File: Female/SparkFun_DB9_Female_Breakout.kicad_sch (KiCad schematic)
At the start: 9 parts, among them J1 DB9-Female, J2 Conn_01x09, J3 Conn_01x01, J4 Conn_01x01

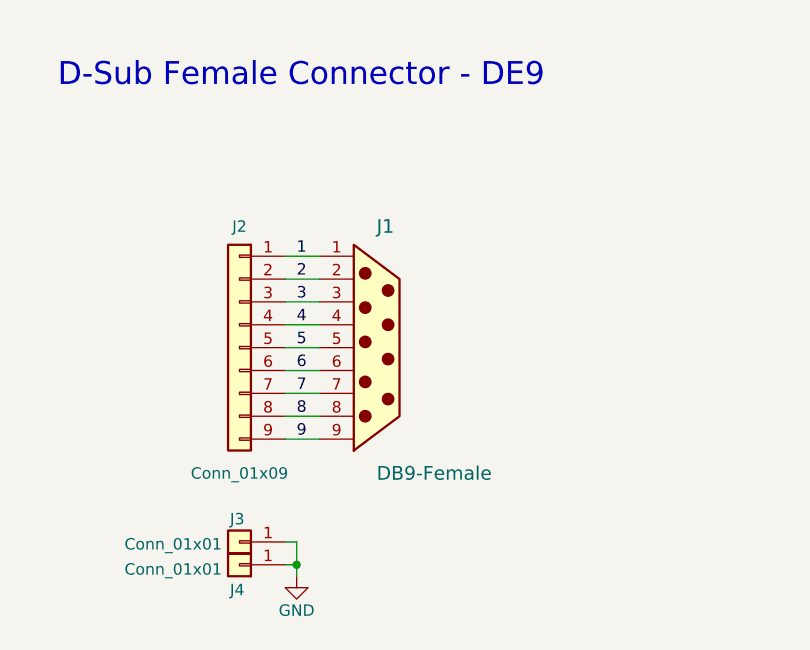
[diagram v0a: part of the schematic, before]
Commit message: Updates DE9 symbol
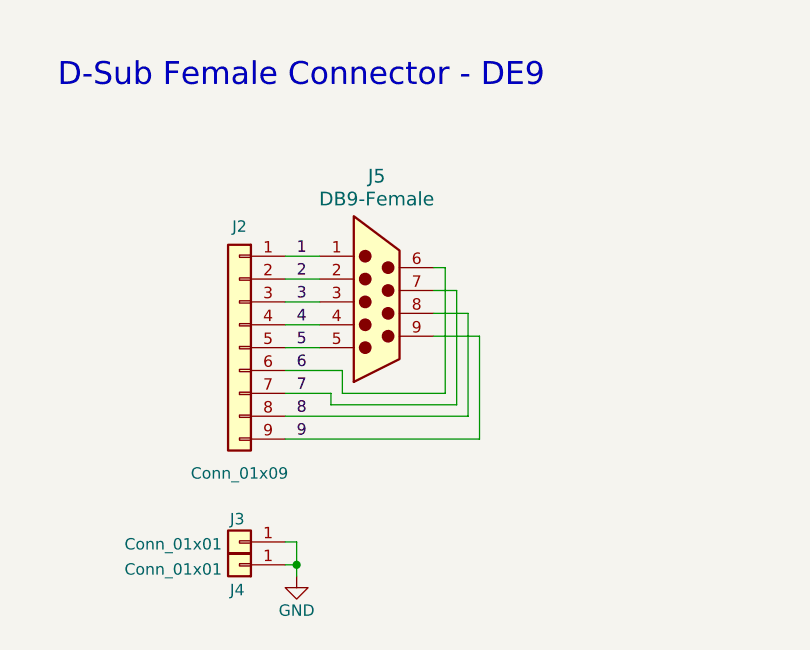
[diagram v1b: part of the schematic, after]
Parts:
- removed J1: DB9-Female, DE9_Footprint:DB9_Female, symbol DB9-Female:DB9 Female
- added J5: DB9-Female, DE9_Footprint:DB9_Female, symbol DB9-Female:DB9 Female
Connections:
- net 1: now also J5.1
- net 2: now also J5.2
- net 3: now also J5.3
- net 4: now also J5.4
- net 5: now also J5.5
- net 6: now also J5.6
- net 7: now also J5.7
- net 8: now also J5.8
- net 9: now also J5.9
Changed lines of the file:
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@@
+	(wire
+		(pts
+			(xy 88.9 99.06) (xy 88.9 86.36)
+		)
+		(stroke
+			(width 0)
+			(type default)
+		)
+	)
+	(wire
+		(pts
+			(xy 86.36 88.9) (xy 90.17 88.9)
+		)
+		(stroke
+			(width 0)
+			(type default)
+		)
+	)
 	(wire
 		(pts
@@
 	(wire
 		(pts
-			(xy 69.85 100.33) (xy 73.66 100.33)
+			(xy 69.85 100.33) (xy 90.17 100.33)
+		)
+		(stroke
+			(width 0)
+			(type default)
+		)
+	)
+	(wire
+		(pts
+			(xy 90.17 88.9) (xy 90.17 100.33)
+		)
+		(stroke
+			(width 0)
+			(type default)
+		)
+	)
+	(wire
+		(pts
+			(xy 74.93 97.79) (xy 74.93 99.06)
 		)
 		(stroke
@@
 	(wire
 		(pts
-			(xy 69.85 102.87) (xy 73.66 102.87)
+			(xy 69.85 102.87) (xy 91.44 102.87)
 		)
 		(stroke
@@
 	(wire
 		(pts
-			(xy 69.85 97.79) (xy 73.66 97.79)
-		)
-		(stroke
-			(width 0)
-			(type default)
-		)
-	)
-	(wire
-		(pts
-			(xy 69.85 95.25) (xy 73.66 95.25)
+			(xy 69.85 97.79) (xy 74.93 97.79)
+		)
+		(stroke
+			(width 0)
+			(type default)
+		)
+	)
+	(wire
+		(pts
+			(xy 91.44 91.44) (xy 86.36 91.44)
+		)
+		(stroke
+			(width 0)
+			(type default)
+		)
+	)
+	(wire
+		(pts
+			(xy 69.85 95.25) (xy 76.2 95.25)
+		)
+		(stroke
+			(width 0)
+			(type default)
+		)
+	)
+	(wire
+		(pts
+			(xy 87.63 97.79) (xy 76.2 97.79)
+		)
+		(stroke
+			(width 0)
+			(type default)
+		)
+	)
+	(wire
+		(pts
+			(xy 76.2 97.79) (xy 76.2 95.25)
+		)
+		(stroke
+			(width 0)
+			(type default)
+		)
+	)
+	(wire
+		(pts
+			(xy 86.36 83.82) (xy 87.63 83.82)
+		)
+		(stroke
+			(width 0)
+			(type default)
+		)
+	)
+	(wire
+		(pts
+			(xy 88.9 86.36) (xy 86.36 86.36)
 		)
 		(stroke
@@
 	(wire
 		(pts
+			(xy 87.63 83.82) (xy 87.63 97.79)
+		)
+		(stroke
+			(width 0)
+			(type default)
+		)
+	)
+	(wire
+		(pts
 			(xy 71.12 114.3) (xy 71.12 116.84)
 		)
@@
 		(pts
 			(xy 69.85 85.09) (xy 73.66 85.09)
+		)
+		(stroke
+			(width 0)
+			(type default)
+		)
+	)
+	(wire
+		(pts
+			(xy 91.44 102.87) (xy 91.44 91.44)
+		)
+		(stroke
+			(width 0)
+			(type default)
+		)
+	)
+	(wire
+		(pts
+			(xy 74.93 99.06) (xy 88.9 99.06)
 		)
 		(stroke
@@
 	)
 	(symbol
+		(lib_name "DB9 Female_1")
+		(lib_id "DB9-Female:DB9 Female")
+		(at 80.01 88.9 0)
+		(unit 1)
+		(exclude_from_sim no)
+		(in_bom yes)
+		(on_board yes)
+		(dnp no)
+		(fields_autoplaced yes)
+		(property "Reference" "J5"
+			(at 80.01 73.66 0)
+			(effects
+				(font
+					(size 1.524 1.524)
+				)
+			)
+		)
+		(property "Value" "DB9-Female"
+			(at 80.01 76.2 0)
+			(effects
+				(font
+					(size 1.524 1.524)
+				)
+			)
+		)
+		(property "Footprint" "DE9_Footprint:DB9_Female"
+			(at 80.01 105.156 0)
+			(effects
+				(font
+					(size 1.27 1.27)
+					(italic yes)
+				)
+				(hide yes)
+			)
+		)
+		(property "Datasheet" "https://www.lcsc.com/datasheet/lcsc_datasheet_2411220417_XUNPU-D-SUB-DR-9PCM-CB_C19077337.pdf"
+			(at 80.01 107.696 0)
+			(effects
+				(font
+					(size 1.27 1.27)
+					(italic yes)
+				)
+				(hide yes)
+			)
+		)
+		(property "Description" ""
+			(at 80.01 88.9 0)
+			(effects
+				(font
+					(size 1.27 1.27)
+				)
+				(hide yes)
+			)
+		)
+		(pin "6"
+		)
+		(pin "3"
+		)
+		(pin "5"
+		)
+		(pin "4"
+		)
+		(pin "2"
+		)
+		(pin "1"
+		)
+		(pin "8"
+		)
+		(pin "7"
+		)
+		(pin "9"
+		)
+		(instances
+			(project ""
+				(path "/e3dd3ae4-244d-4cba-9cca-5d2abf83f29a"
+					(reference "J5")
+					(unit 1)
+				)
+			)
+		)
+	)
+	(symbol
 		(lib_id "SparkFun-Connector:Conn_01x09")
 		(at 64.77 92.71 0)
@@
 					(unit 1)
 				)
-			)
-		)
-	)
-	(symbol
-		(lib_id "DB9-Female:DB9 Female")
-		(at 80.01 92.71 0)
-		(unit 1)
-		(exclude_from_sim no)
-		(in_bom yes)
-		(on_board yes)
-		(dnp no)
-		(property "Reference" "J1"
-			(at 80.01 79.248 0)
-			(effects
-				(font
-					(size 1.524 1.524)
-				)
-				(justify left)
-			)
-		)
-		(property "Value" "DB9-Female"
-			(at 80.01 106.68 0)
-			(effects
-				(font
-					(size 1.524 1.524)
-				)
-				(justify left)
-			)
-		)
-		(property "Footprint" "DE9_Footprint:DB9_Female"
-			(at 80.01 108.966 0)
-			(effects
-				(font
-					(size 1.27 1.27)
-					(italic yes)
-				)
-				(hide yes)
-			)
-		)
-		(property "Datasheet" "https://www.lcsc.com/datasheet/lcsc_datasheet_2411220417_XUNPU-D-SUB-DR-9PCM-CB_C19077337.pdf"
-			(at 80.01 111.506 0)
-			(effects
-				(font
-					(size 1.27 1.27)
-					(italic yes)
-				)
-				(hide yes)
-			)
-		)
-		(property "Description" ""
-			(at 80.01 92.71 0)
-			(effects
-				(font
-					(size 1.27 1.27)
-				)
-				(hide yes)
-			)
-		)
-		(pin "9"
-		)
-		(pin "8"
-		)
-		(pin "4"
-		)
-		(pin "7"
-		)
-		(pin "6"
-		)
-		(pin "3"
-		)
-		(pin "5"
-		)
-		(pin "2"
-		)
-		(pin "1"
-		)
-		(instances
-			(project ""
-				(path "/e3dd3ae4-244d-4cba-9cca-5d2abf83f29a"
-					(reference "J1")
-					(unit 1)
-				)
